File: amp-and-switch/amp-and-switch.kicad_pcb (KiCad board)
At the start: 2 copper layers, 40.4 x 16.5 mm, 28 parts, among them J1 Conn_01x05, J2 Conn_01x01, J3 Conn_01x04, J4 Conn_01x03, J5 Conn_01x01, Q1 MMBT3904, Q2 MMBT3904, U1 LM324

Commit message: Fixed a missed ground trace on the switch board.
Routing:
- net GND: track 12.4 -> 13.8 mm, vias 3 -> 4
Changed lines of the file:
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@@
     (thickness 1.6)
     (drawings 11)
-    (tracks 169)
+    (tracks 171)
     (zones 0)
     (modules 28)
@@
     (solder_mask_min_width 0.25)
     (aux_axis_origin 0 0)
-    (visible_elements FFFFFF7F)
+    (visible_elements 7FFFFFFF)
     (pcbplotparams
       (layerselection 0x010fc_ffffffff)
@@
   (via (at 105.918 91.186) (size 0.8) (drill 0.4) (layers F.Cu B.Cu) (net 2))
   (segment (start 104.394 91.186) (end 105.918 91.186) (width 0.25) (layer F.Cu) (net 2))
+  (via (at 115.697 80.264) (size 0.8) (drill 0.4) (layers F.Cu B.Cu) (net 2))
+  (segment (start 115.697 81.652) (end 115.697 80.264) (width 0.25) (layer F.Cu) (net 2))
   (segment (start 104.394 83.294) (end 104.122 83.566) (width 0.25) (layer F.Cu) (net 3))
   (segment (start 104.394 80.772) (end 104.394 83.294) (width 0.25) (layer F.Cu) (net 3))

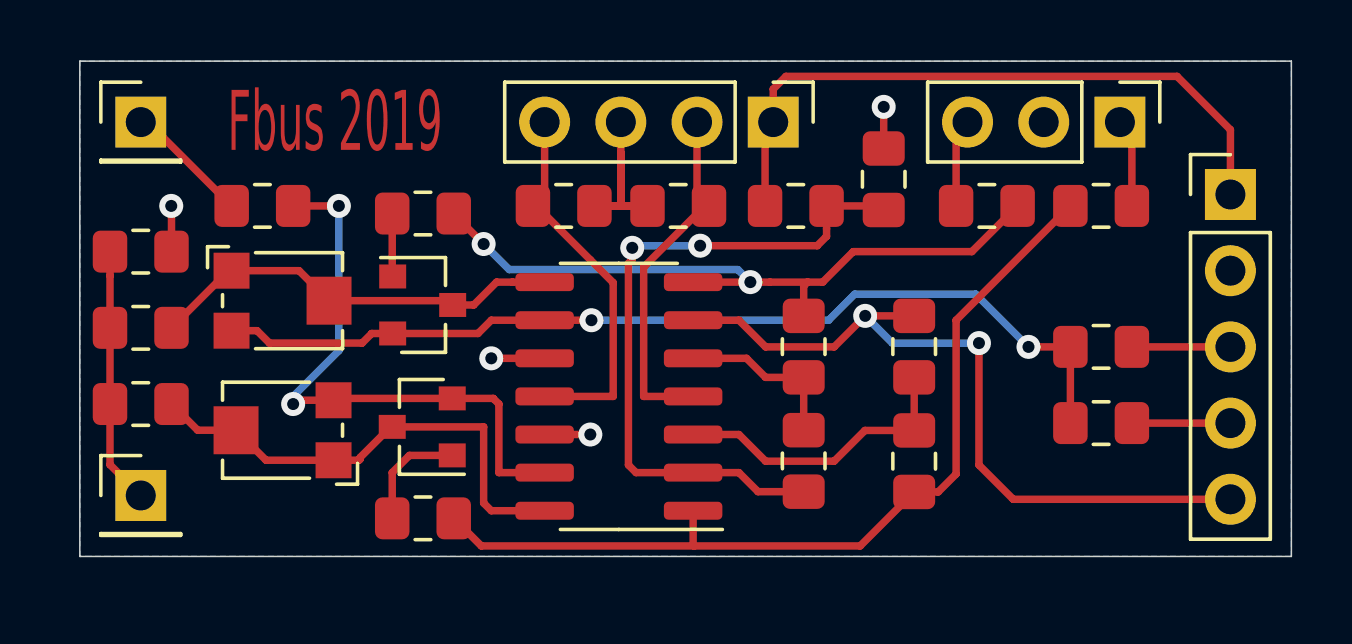
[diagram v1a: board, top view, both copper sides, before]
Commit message: Updated both the amp-and-switch board and the power-board-12v board to version 0.2 after performing bring-up and fixing many issues.
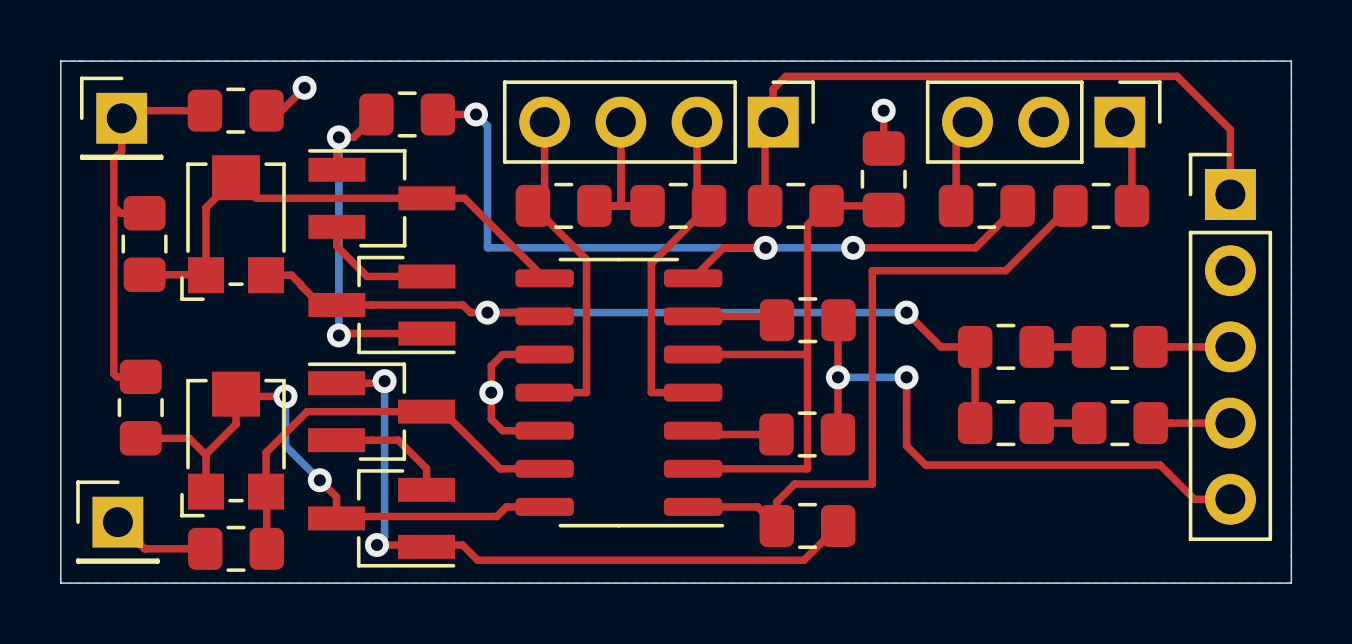
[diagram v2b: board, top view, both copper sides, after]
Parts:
- removed R3, R4: 20K, Resistor_SMD:R_0805_2012Metric_Pad1.15x1.40mm_HandSolder
- added C3: 100 nF, Capacitor_SMD:C_0805_2012Metric_Pad1.15x1.40mm_HandSolder, F.Cu at (123.6, 88.3)
- added C4: 100 nF, Capacitor_SMD:C_0805_2012Metric_Pad1.15x1.40mm_HandSolder, F.Cu at (123.6, 90.8)
- added Q3: Q_NMOS_GSD, Package_TO_SOT_SMD:SOT-23_Handsoldering, F.Cu at (99.0, 83.3)
- added Q4: Q_NMOS_GSD, Package_TO_SOT_SMD:SOT-23_Handsoldering, F.Cu at (99.0, 86.9)
- C1, C2: value 100nF -> 100 nF
- Q1, Q2: value MMBT3904 -> Q_NMOS_GSD; footprint Package_TO_SOT_SMD:SOT-23 -> Package_TO_SOT_SMD:SOT-23_Handsoldering
- R12, R15: value 1K -> 3K
- moved J2 13.4 mm to (90.2, 94.1)
- moved R5 12.8 mm to (113.2, 94.2), turned to 180 degrees
- moved J5 12.6 mm to (90.3, 80.6)
- moved R6 11.5 mm to (94.1, 95.0)
- moved R16 5.67 mm to (94.1, 80.4)
- moved R2 4.69 mm to (113.2, 87.4), turned to 0 degrees
- moved R1 4.61 mm to (113.1, 91.2), turned to 0 degrees
- moved Q2 3.81 mm to (99.0, 90.4)
- moved R9 3.34 mm to (99.8, 80.5)
- moved Q1 3.34 mm to (99.0, 94.0)
- moved R10 3.17 mm to (119.8, 88.3)
- moved R11 3.17 mm to (119.8, 90.8)
- moved RV2 3.12 mm to (94.1, 84.1), turned to 90 degrees
- moved R15 2.80 mm to (91.1, 84.8), turned to 270 degrees
- moved RV1 1.47 mm to (94.1, 91.3), turned to 90 degrees
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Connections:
- J1 pad 3: Net-(J1-Pad3) -> Net-(C3-Pad2)
- J1 pad 4: Net-(J1-Pad4) -> Net-(C4-Pad2)
- Q2 pad 1: Net-(Q2-Pad1) -> Net-(Q1-Pad1)
- Q2 pad 2: Net-(Q2-Pad2) -> Net-(Q1-Pad2)
- R10 pad 1: Net-(Q2-Pad2) -> Net-(Q4-Pad3)
- R10 pad 2: Net-(J1-Pad3) -> Net-(C3-Pad1)
- R11 pad 1: Net-(Q2-Pad2) -> Net-(Q4-Pad3)
- R11 pad 2: Net-(J1-Pad4) -> Net-(C4-Pad1)
- R15 pad 2: Net-(Q2-Pad3) -> Net-(Q3-Pad3)
- R2 pad 2: +2V5 -> Net-(J1-Pad5)
- R6 pad 1: Net-(Q1-Pad2) -> Net-(Q2-Pad3)
- R9 pad 1: Net-(Q2-Pad1) -> Net-(Q3-Pad1)
- RV1 pad 3: Net-(Q1-Pad2) -> Net-(Q2-Pad3)
- RV2 pad 1: Net-(Q2-Pad3) -> Net-(Q3-Pad3)
- RV2 pad 2: Net-(Q2-Pad3) -> Net-(Q3-Pad3)
- RV2 pad 3: Net-(Q2-Pad2) -> Net-(Q4-Pad3)
- U1 pad 13: Net-(Q1-Pad2) -> Net-(Q2-Pad3)
- U1 pad 5: Net-(R2-Pad1) -> +2V5
- U1 pad 6: Net-(J1-Pad5) -> Net-(R2-Pad1)
- U1 pad 8: Net-(Q2-Pad3) -> Net-(Q3-Pad3)
- U1 pad 9: Net-(Q2-Pad2) -> Net-(Q4-Pad3)
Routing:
- net Net-(Q2-Pad2): track 32.1 -> 0.00 mm, vias 2 -> 0
- net Net-(Q4-Pad3): track 0.00 -> 29.1 mm, vias 0 -> 2
- net Net-(Q1-Pad1): track 3.76 -> 23.3 mm, vias 0 -> 2
- net Net-(Q3-Pad3): track 0.00 -> 17.4 mm
- net Net-(Q1-Pad2): track 19.6 -> 4.04 mm, vias 2 -> 0
- net Net-(Q3-Pad1): track 0.00 -> 12.2 mm, vias 0 -> 2
- net /RadioMute: track 29.8 -> 21.9 mm
- net Net-(R1-Pad1): track 9.93 -> 2.83 mm
- net Net-(J1-Pad5): track 25.3 -> 19.9 mm
- net Net-(J5-Pad1): track 8.55 -> 13.5 mm
- net +2V5: track 22.7 -> 18.2 mm, vias 2 -> 0
- net Net-(Q3-Pad2): track 0.00 -> 4.07 mm
- net Net-(J1-Pad4): track 3.28 -> 0.00 mm
- net Net-(J1-Pad3): track 3.28 -> 0.00 mm
- net Net-(Q1-Pad3): track 16.4 -> 19.5 mm, vias 0 -> 2
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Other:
- board size 40.4 x 16.5 mm -> 41 x 17.4 mm
- board text added: "Ole Radio Input Switch Amp and Switch Board Version 0.2"
- board text removed: "Ole Radio Input Switch Amp and Switch Board Version 0.1"
